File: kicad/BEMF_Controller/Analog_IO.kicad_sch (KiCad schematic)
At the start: 44 parts, among them U10 OPA2376AIDR, U11 ADC108S022CIMTX/NOPB, U12 OPA2376AIDR, U16 OPA2376AIDR

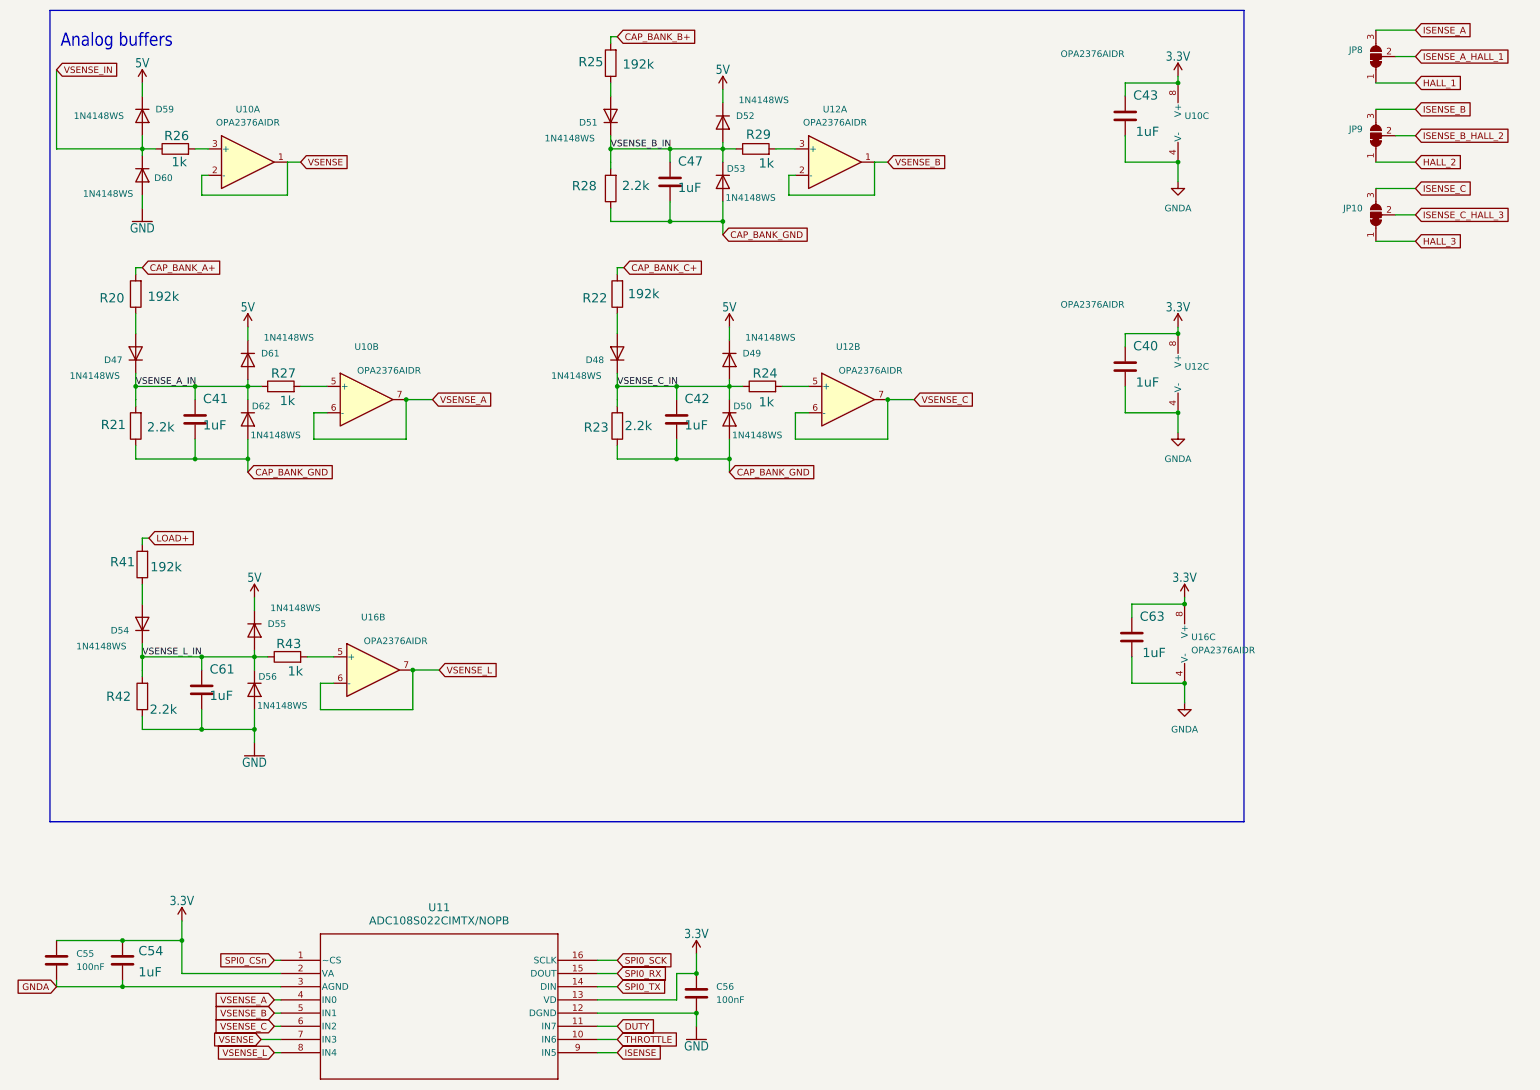
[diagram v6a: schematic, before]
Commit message: Change of plans. Make simple controller for MEG only
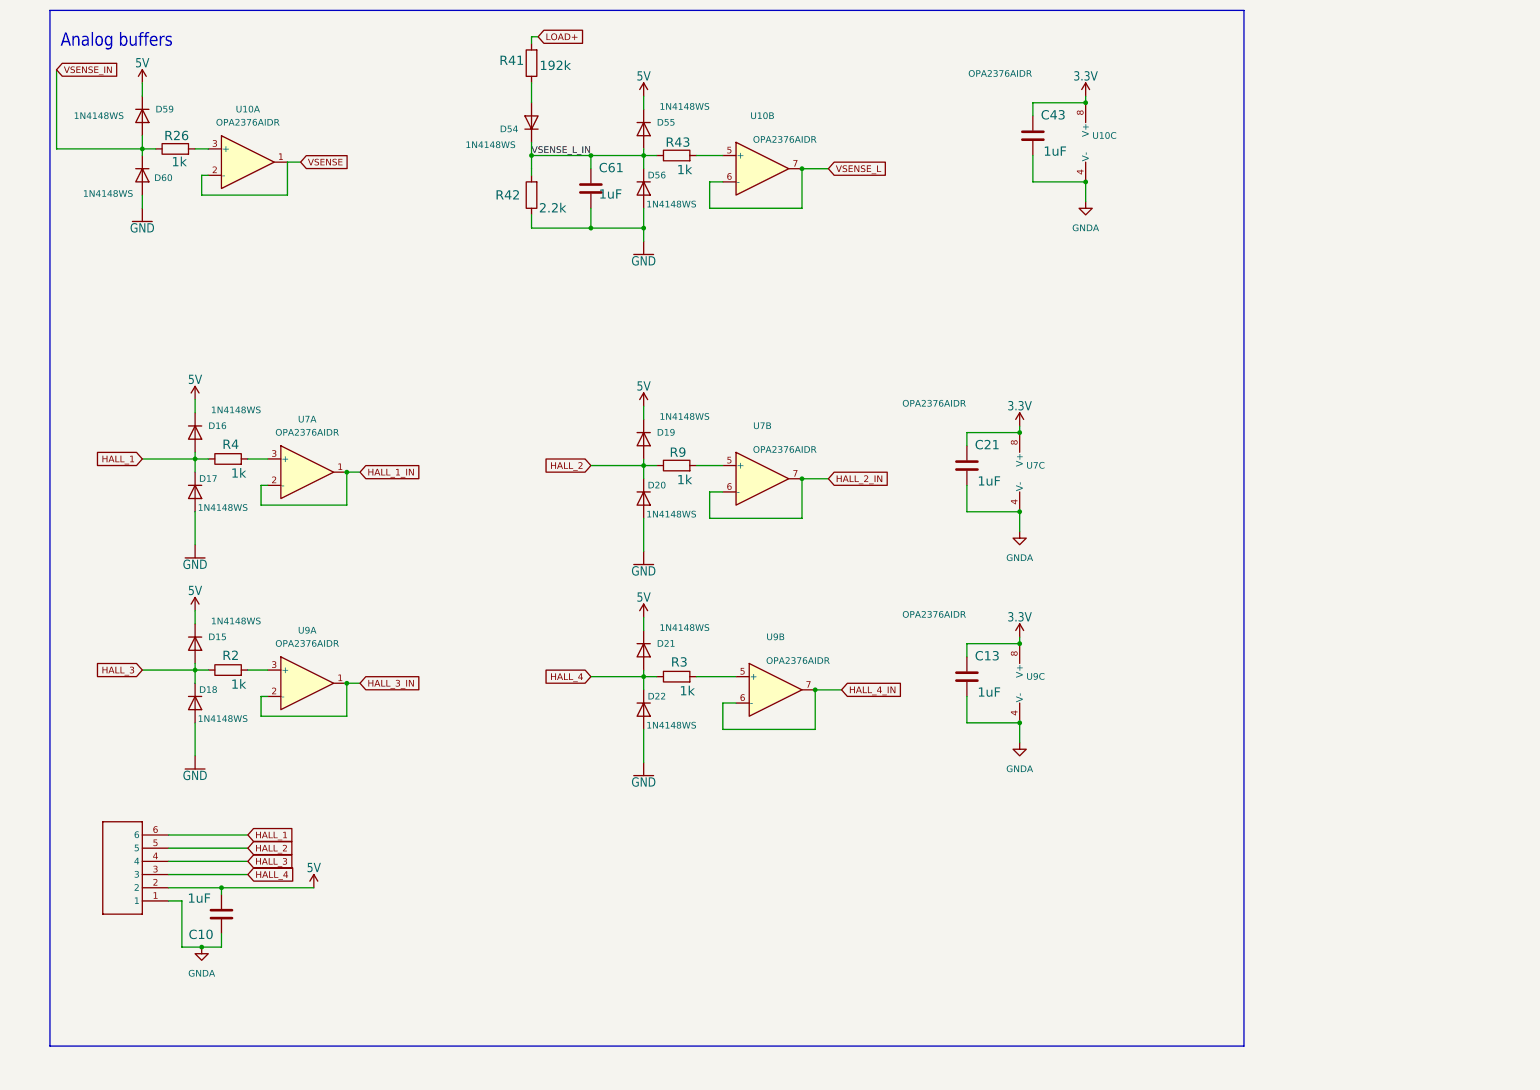
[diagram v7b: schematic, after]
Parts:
- removed C40, C41, C42, C47, C54, C63: 1uF, Capacitor_SMD:C_1812_4532Metric, symbol Component_Library:CHV1812N250105MXT
- removed C55, C56: 100nF, Capacitor_SMD:C_1210_3225Metric_Pad1.33x2.70mm_HandSolder, symbol Device:C
- removed D47, D48, D49, D50, D51, D52, D53, D61, D62: 1N4148WS, Diode_SMD:D_SOD-323, symbol Diode:1N4148WS
- removed JP10, JP8, JP9: SolderJumper_3_Bridged12, Jumper:SolderJumper-3_P1.3mm_Bridged2Bar12_RoundedPad1.0x1.5mm, symbol Jumper:SolderJumper_3_Bridged12
- removed R20, R22, R25: 192k, Resistor_SMD:R_1206_3216Metric, symbol Component_Library:R192k
- removed R21, R23, R28: 2.2k, Resistor_SMD:R_1206_3216Metric, symbol Component_Library:R2k2
- removed R24, R27, R29: 1k, Resistor_SMD:R_1206_3216Metric, symbol Component_Library:R1k
- removed U11: ADC108S022CIMTX/NOPB, footprints:MTC16, symbol Component_Library:ADC108S022CIMTX_NOPB
- removed U12, U16: OPA2376AIDR, footprints:D8, symbol Component_Library:OPA2376AIDR
- added C10, C13, C21: 1uF, Capacitor_SMD:C_1812_4532Metric, symbol Component_Library:CHV1812N250105MXT
- added D15, D16, D17, D18, D19, D20, D21, D22: 1N4148WS, Diode_SMD:D_SOD-323, symbol Diode:1N4148WS
- added J4: HEADER6, main:6PINVALULOK, symbol main-eagle-import:HEADER6
- added R2, R3, R4, R9: 1k, Resistor_SMD:R_1206_3216Metric, symbol Component_Library:R1k
- added U7, U9: OPA2376AIDR, footprints:D8, symbol Component_Library:OPA2376AIDR
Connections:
- net VSENSE_A is gone; now on net VSENSE_L: U10.6 (-), U10.7
- net 3.3V: now also C13.1, C21.1, U7.8 (V+), U9.8 (V+)
- net 5V: now also C10.2, D15.1 (K), D16.1 (K), D19.1 (K), D21.1 (K), J4.2
- net GND: now also D17.2 (A), D18.2 (A), D20.2 (A), D22.2 (A)
- net GNDA: now also C10.1, C13.2, C21.2, J4.1, U7.4 (V-), U9.4 (V-)
- net HALL_1: now also D16.2 (A), D17.1 (K), J4.6, R4.1
- net HALL_2: now also D19.2 (A), D20.1 (K), J4.5, R9.1
- net HALL_3: now also D15.2 (A), D18.1 (K), J4.4, R2.1
- net at U10.5 (+): now also R43.2
- new net: R9.2, U7.5 (+)
- new net: R4.2, U7.3 (+)
- new net: R2.2, U9.3 (+)
- new net: R3.2, U9.5 (+)
- new net HALL_1_IN: U7.1, U7.2 (-)
- new net HALL_2_IN: U7.6 (-), U7.7
- new net HALL_3_IN: U9.1, U9.2 (-)
- new net HALL_4: D21.2 (A), D22.1 (K), J4.3, R3.1
- new net HALL_4_IN: U9.6 (-), U9.7
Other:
- moved on the sheet: C43, C61, D54, D55, D56, R41, R42, R43, U10B, U10C

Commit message: Pretty much complete, but a few things left to do.
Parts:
- removed D54: 1N4148WS, Diode_SMD:D_SOD-323, symbol Diode:1N4148WS
- added C29: 1uF, Capacitor_SMD:C_1812_4532Metric, symbol Component_Library:CHV1812N250105MXT
- J4: footprint main:6PINVALULOK -> TerminalBlock_Phoenix:TerminalBlock_Phoenix_MKDS-1,5-6_1x06_P5.00mm_Horizontal
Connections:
- net GND: now also C29.2
- net VSENSE_L_IN: now also R41.1, C29.1
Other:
- moved on the sheet: C61, R41
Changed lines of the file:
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@@
 	)
 	(junction
-		(at 110.49 43.18)
+		(at 105.41 43.18)
 		(diameter 0)
 		(color 0 0 0 0)
 	)
 	(junction
-		(at 99.06 29.21)
+		(at 105.41 29.21)
 		(diameter 0)
 		(color 0 0 0 0)
 	)
 	(junction
-		(at 110.49 29.21)
+		(at 99.06 29.21)
 		(diameter 0)
 		(color 0 0 0 0)
@@
 	)
 	(junction
+		(at 113.03 29.21)
+		(diameter 0)
+		(color 0 0 0 0)
+	)
+	(junction
 		(at 151.13 91.44)
 		(diameter 0)
@@
 	)
 	(junction
+		(at 113.03 43.18)
+		(diameter 0)
+		(color 0 0 0 0)
+	)
+	(junction
 		(at 120.65 129.54)
 		(diameter 0)
@@
 	(wire
 		(pts
-			(xy 99.06 29.21) (xy 110.49 29.21)
+			(xy 99.06 29.21) (xy 105.41 29.21)
 		)
 		(stroke
@@
 	(wire
 		(pts
-			(xy 110.49 31.75) (xy 110.49 29.21)
+			(xy 105.41 31.75) (xy 105.41 29.21)
 		)
 		(stroke
@@
 	(wire
 		(pts
-			(xy 110.49 43.18) (xy 99.06 43.18)
+			(xy 105.41 43.18) (xy 113.03 43.18)
 		)
 		(stroke
@@
 	(wire
 		(pts
+			(xy 105.41 43.18) (xy 99.06 43.18)
+		)
+		(stroke
+			(width 0)
+			(type default)
+		)
+	)
+	(wire
+		(pts
 			(xy 34.29 128.27) (xy 34.29 130.81)
 		)
@@
 	(wire
 		(pts
-			(xy 99.06 6.35) (xy 99.06 7.62)
+			(xy 99.06 13.97) (xy 99.06 15.24)
 		)
 		(stroke
@@
 	(wire
 		(pts
-			(xy 110.49 43.18) (xy 120.65 43.18)
-		)
-		(stroke
-			(width 0)
-			(type default)
-		)
-	)
-	(wire
-		(pts
 			(xy 110.49 88.9) (xy 120.65 88.9)
 		)
@@
 	(wire
 		(pts
-			(xy 110.49 29.21) (xy 120.65 29.21)
+			(xy 182.88 125.73) (xy 182.88 123.19)
 		)
 		(stroke
@@
 	(wire
 		(pts
-			(xy 182.88 125.73) (xy 182.88 123.19)
+			(xy 120.65 39.37) (xy 120.65 43.18)
 		)
 		(stroke
@@
 	(wire
 		(pts
-			(xy 120.65 39.37) (xy 120.65 43.18)
+			(xy 113.03 29.21) (xy 120.65 29.21)
 		)
 		(stroke
@@
 	(wire
 		(pts
+			(xy 113.03 43.18) (xy 120.65 43.18)
+		)
+		(stroke
+			(width 0)
+			(type default)
+		)
+	)
+	(wire
+		(pts
 			(xy 63.5 130.81) (xy 66.04 130.81)
 		)
@@
 	(wire
 		(pts
-			(xy 99.06 6.35) (xy 100.33 6.35)
+			(xy 99.06 13.97) (xy 100.33 13.97)
+		)
+		(stroke
+			(width 0)
+			(type default)
+		)
+	)
+	(wire
+		(pts
+			(xy 113.03 29.21) (xy 113.03 31.75)
 		)
 		(stroke
@@
 	(wire
 		(pts
-			(xy 99.06 15.24) (xy 99.06 19.05)
+			(xy 99.06 22.86) (xy 99.06 26.67)
 		)
 		(stroke
@@
 	(wire
 		(pts
+			(xy 113.03 39.37) (xy 113.03 43.18)
+		)
+		(stroke
+			(width 0)
+			(type default)
+		)
+	)
+	(wire
+		(pts
 			(xy 24.13 87.63) (xy 34.29 87.63)
 		)
@@
 	(wire
 		(pts
-			(xy 110.49 39.37) (xy 110.49 43.18)
+			(xy 105.41 39.37) (xy 105.41 43.18)
+		)
+		(stroke
+			(width 0)
+			(type default)
+		)
+	)
+	(wire
+		(pts
+			(xy 105.41 29.21) (xy 113.03 29.21)
 		)
 		(stroke
@@
 	(global_label "LOAD+"
 		(shape input)
-		(at 100.33 6.35 0)
+		(at 100.33 13.97 0)
 		(fields_autoplaced yes)
 		(effects
@@
 		)
 		(property "Intersheetrefs" "${INTERSHEET_REFS}"
-			(at 109.6048 6.35 0)
+			(at 109.6048 13.97 0)
 			(effects
 				(font
@@
 	(symbol
 		(lib_id "Component_Library:R192k")
-		(at 99.06 11.43 180)
+		(at 99.06 19.05 180)
 		(unit 1)
 		(exclude_from_sim no)
@@
 		(dnp no)
 		(property "Reference" "R41"
-			(at 95.25 9.906 0)
+			(at 95.25 17.526 0)
 			(effects
 				(font
@@
 		)
 		(property "Value" "192k"
-			(at 103.632 12.954 0)
+			(at 103.632 20.574 0)
 			(effects
 				(font
@@
 		)
 		(property "Footprint" "Resistor_SMD:R_1206_3216Metric"
-			(at 100.838 11.43 90)
+			(at 100.838 19.05 90)
 			(effects
 				(font
@@
 		)
 		(property "Datasheet" "~"
-			(at 99.06 11.43 0)
+			(at 99.06 19.05 0)
 			(effects
 				(font
@@
 		)
 		(property "Description" "Resistor"
-			(at 99.06 11.43 0)
+			(at 99.06 19.05 0)
 			(effects
 				(font
@@
 	(symbol
 		(lib_id "Component_Library:CHV1812N250105MXT")
-		(at 110.49 35.56 0)
+		(at 105.41 35.56 0)
 		(unit 1)
 		(exclude_from_sim no)
@@
 		(dnp no)
 		(property "Reference" "C61"
-			(at 112.014 32.639 0)
+			(at 106.934 32.639 0)
 			(effects
 				(font
@@
 		)
 		(property "Value" "1uF"
-			(at 112.014 37.719 0)
+			(at 107.442 39.624 0)
 			(effects
 				(font
@@
 		)
 		(property "Footprint" "Capacitor_SMD:C_1812_4532Metric"
-			(at 111.4552 39.37 0)
+			(at 106.3752 39.37 0)
 			(effects
 				(font
@@
 		)
 		(property "Datasheet" "https://88ce57.p3cdn1.secureserver.net/wp-content/uploads/2023/01/chv_series-1.pdf"
-			(at 110.49 35.56 0)
+			(at 105.41 35.56 0)
 			(effects
 				(font
@@
 		)
 		(property "Description" "HVCAP1812 X7R 1UF 20% 250V"
-			(at 110.49 35.56 0)
+			(at 105.41 35.56 0)
 			(effects
 				(font
@@
 	)
 	(symbol
-		(lib_id "Diode:1N4148WS")
-		(at 99.06 22.86 90)
-		(unit 1)
-		(exclude_from_sim no)
-		(in_bom yes)
-		(on_board yes)
-		(dnp no)
-		(property "Reference" "D54"
-			(at 96.52 24.1301 90)
-			(effects
-				(font
-					(size 1.27 1.27)
-				)
-				(justify left)
-			)
-		)
-		(property "Value" "1N4148WS"
-			(at 96.012 27.178 90)
-			(effects
-				(font
-					(size 1.27 1.27)
-				)
-				(justify left)
-			)
-		)
-		(property "Footprint" "Diode_SMD:D_SOD-323"
-			(at 103.505 22.86 0)
-			(effects
-				(font
-					(size 1.27 1.27)
-				)
-				(hide yes)
-			)
-		)
-		(property "Datasheet" "https://www.vishay.com/docs/85751/1n4148ws.pdf"
-			(at 99.06 22.86 0)
-			(effects
-				(font
-					(size 1.27 1.27)
-				)
-				(hide yes)
-			)
-		)
-		(property "Description" "75V 0.15A Fast switching Diode, SOD-323"
-			(at 99.06 22.86 0)
-			(effects
-				(font
-					(size 1.27 1.27)
-				)
-				(hide yes)
-			)
-		)
-		(property "Sim.Device" "D"
-			(at 99.06 22.86 0)
-			(effects
-				(font
-					(size 1.27 1.27)
-				)
-				(hide yes)
-			)
-		)
-		(property "Sim.Pins" "1=K 2=A"
-			(at 99.06 22.86 0)
-			(effects
-				(font
-					(size 1.27 1.27)
-				)
-				(hide yes)
-			)
-		)
-		(pin "1"
-		)
-		(pin "2"
-		)
-		(instances
-			(project "BEMF_Controller"
-				(path "/80a514a6-29a9-4699-8a7d-cff678a7ed07/6990bf25-70eb-45d9-b265-2461b625100e"
-					(reference "D54")
-					(unit 1)
-				)
-			)
-		)
-	)
-	(symbol
 		(lib_id "Component_Library:R1k")
 		(at 40.64 87.63 90)
@@
 			)
 		)
-		(property "Footprint" "main:6PINVALULOK"
+		(property "Footprint" "TerminalBlock_Phoenix:TerminalBlock_Phoenix_MKDS-1,5-6_1x06_P5.00mm_Horizontal"
 			(at 19.05 165.1 0)
 			(effects
@@
 					(unit 1)
 				)
+			)
+		)
+	)
+	(symbol
+		(lib_id "Component_Library:CHV1812N250105MXT")
+		(at 113.03 35.56 0)
+		(unit 1)
+		(exclude_from_sim no)
+		(in_bom yes)
+		(on_board yes)
+		(dnp no)
+		(property "Reference" "C29"
+			(at 114.554 32.639 0)
+			(effects
+				(font
+					(size 1.778 1.778)
+				)
+				(justify left bottom)
+			)
+		)
+		(property "Value" "1uF"
+			(at 115.316 39.624 0)
+			(effects
+				(font
+					(size 1.778 1.778)
+				)
+				(justify left bottom)
+			)
+		)
+		(property "Footprint" "Capacitor_SMD:C_1812_4532Metric"
+			(at 113.9952 39.37 0)
+			(effects
+				(font
+					(size 1.27 1.27)
+				)
+				(hide yes)
+			)
+		)
+		(property "Datasheet" "https://88ce57.p3cdn1.secureserver.net/wp-content/uploads/2023/01/chv_series-1.pdf"
+			(at 113.03 35.56 0)
+			(effects
+				(font
+					(size 1.27 1.27)
+				)
+				(hide yes)
+			)
+		)
+		(property "Description" "HVCAP1812 X7R 1UF 20% 250V"
+			(at 113.03 35.56 0)
+			(effects
+				(font
+					(size 1.27 1.27)
+				)
+				(hide yes)
+			)
+		)
+		(pin "1"
+		)
+		(pin "2"
+		)
+		(instances
+			(project "MEG_Controller"
+				(path "/80a514a6-29a9-4699-8a7d-cff678a7ed07/6990bf25-70eb-45d9-b265-2461b625100e"
+					(reference "C29")
+					(unit 1)
+				)
